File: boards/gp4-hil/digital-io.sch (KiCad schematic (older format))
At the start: 60 parts, among them Q1 SSM6N58NU, Q10 SSM6N58NU, Q2 SSM6N58NU, Q3 SSM6N58NU, Q4 SSM6N58NU, Q5 SSM6N58NU, Q6 SSM6N58NU, Q7 SSM6N58NU, Q8 SSM6N58NU, Q9 SSM6N58NU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

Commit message: Began work on footprint creation for layout.
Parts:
- C57, C58, C59, C60, C61: footprint (none) -> azonenberg_pcb:EIA_0402_CAP_NOSILK
- C62: footprint (none) -> azonenberg_pcb:EIA_0603_CAP_NOSILK
- D1: footprint (none) -> azonenberg_pcb:EIA_0402_LED
- D10, D11, D12, D13, D14, D15, D16, D17, D18, D19, D2, D3, D4, D5, D6, D7, D8, D9: footprint (none) -> azonenberg_pcb:EIA_0603_LED
- Q1, Q10, Q2, Q3, Q4, Q5, Q6, Q7, Q8, Q9: footprint (none) -> azonenberg_pcb:DFN_6_0.65MM_2x2MM_GDS

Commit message: Updated PCB with a lot more component footprints
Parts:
- R81, R82, R83, R84, R85, R86, R87, R88, R89, R90, R91, R92, R93, R94, R95, R96, R97, R98, R99: footprint (none) -> azonenberg_pcb:EIA_0402_RES_NOSILK
- U2: footprint (none) -> azonenberg_pcb:BGA_256_17x17_FULLARRAY_1MM
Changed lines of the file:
@@
 Sheet 7 7
 Title "GreenPak Hardware-In-Loop Test Platform"
-Date "2016-05-19"
+Date "2016-05-20"
 Rev "0.1"
 Comp "Andrew Zonenberg"
@@
 F 0 "U2" H 16350 7350 60  0000 L CNN
 F 1 "XC7A100T-1FTG256C" H 16350 7450 60  0000 L CNN
-F 2 "" H 16350 7550 60  0001 C CNN
+F 2 "azonenberg_pcb:BGA_256_17x17_FULLARRAY_1MM" H 16350 7550 60  0001 C CNN
 F 3 "" H 16350 7550 60  0000 C CNN
 	5    16350 7550
@@
 F 0 "U2" H 19350 7350 60  0000 L CNN
 F 1 "XC7A100T-1FTG256C" H 19350 7450 60  0000 L CNN
-F 2 "" H 19350 7550 60  0001 C CNN
+F 2 "azonenberg_pcb:BGA_256_17x17_FULLARRAY_1MM" H 19350 7550 60  0001 C CNN
 F 3 "" H 19350 7550 60  0000 C CNN
 	6    19350 7550
@@
 F 0 "R81" H 2220 10846 50  0000 L CNN
 F 1 "1K" V 2150 10750 50  0000 L CNN
-F 2 "" V 2080 10800 30  0001 C CNN
+F 2 "azonenberg_pcb:EIA_0402_RES_NOSILK" V 2080 10800 30  0001 C CNN
 F 3 "" H 2150 10800 30  0000 C CNN
 	1    2150 10800
@@
 F 0 "R82" H 6970 9946 50  0000 L CNN
 F 1 "220" V 6900 9850 50  0000 L CNN
-F 2 "" V 6830 9900 30  0001 C CNN
+F 2 "azonenberg_pcb:EIA_0402_RES_NOSILK" V 6830 9900 30  0001 C CNN
 F 3 "" H 6900 9900 30  0000 C CNN
 	1    6900 9900
@@
 F 0 "R84" H 7770 9946 50  0000 L CNN
 F 1 "220" V 7700 9850 50  0000 L CNN
-F 2 "" V 7630 9900 30  0001 C CNN
+F 2 "azonenberg_pcb:EIA_0402_RES_NOSILK" V 7630 9900 30  0001 C CNN
 F 3 "" H 7700 9900 30  0000 C CNN
 	1    7700 9900
@@
 F 0 "R86" H 8570 9946 50  0000 L CNN
 F 1 "220" V 8500 9850 50  0000 L CNN
-F 2 "" V 8430 9900 30  0001 C CNN
+F 2 "azonenberg_pcb:EIA_0402_RES_NOSILK" V 8430 9900 30  0001 C CNN
 F 3 "" H 8500 9900 30  0000 C CNN
 	1    8500 9900
@@
 F 0 "R88" H 9370 9946 50  0000 L CNN
 F 1 "220" V 9300 9850 50  0000 L CNN
-F 2 "" V 9230 9900 30  0001 C CNN
+F 2 "azonenberg_pcb:EIA_0402_RES_NOSILK" V 9230 9900 30  0001 C CNN
 F 3 "" H 9300 9900 30  0000 C CNN
 	1    9300 9900
@@
 F 0 "R90" H 10170 9946 50  0000 L CNN
 F 1 "220" V 10100 9850 50  0000 L CNN
-F 2 "" V 10030 9900 30  0001 C CNN
+F 2 "azonenberg_pcb:EIA_0402_RES_NOSILK" V 10030 9900 30  0001 C CNN
 F 3 "" H 10100 9900 30  0000 C CNN
 	1    10100 9900
@@
 F 0 "R92" H 10970 9946 50  0000 L CNN
 F 1 "220" V 10900 9850 50  0000 L CNN
-F 2 "" V 10830 9900 30  0001 C CNN
+F 2 "azonenberg_pcb:EIA_0402_RES_NOSILK" V 10830 9900 30  0001 C CNN
 F 3 "" H 10900 9900 30  0000 C CNN
 	1    10900 9900
@@
 F 0 "R94" H 11770 9946 50  0000 L CNN
 F 1 "220" V 11700 9850 50  0000 L CNN
-F 2 "" V 11630 9900 30  0001 C CNN
+F 2 "azonenberg_pcb:EIA_0402_RES_NOSILK" V 11630 9900 30  0001 C CNN
 F 3 "" H 11700 9900 30  0000 C CNN
 	1    11700 9900
@@
 F 0 "R96" H 12570 9946 50  0000 L CNN
 F 1 "220" V 12500 9850 50  0000 L CNN
-F 2 "" V 12430 9900 30  0001 C CNN
+F 2 "azonenberg_pcb:EIA_0402_RES_NOSILK" V 12430 9900 30  0001 C CNN
 F 3 "" H 12500 9900 30  0000 C CNN
 	1    12500 9900
@@
 F 0 "R98" H 13370 9946 50  0000 L CNN
 F 1 "220" V 13300 9850 50  0000 L CNN
-F 2 "" V 13230 9900 30  0001 C CNN
+F 2 "azonenberg_pcb:EIA_0402_RES_NOSILK" V 13230 9900 30  0001 C CNN
 F 3 "" H 13300 9900 30  0000 C CNN
 	1    13300 9900
@@
 F 0 "R83" H 6970 11246 50  0000 L CNN
 F 1 "220" V 6900 11150 50  0000 L CNN
-F 2 "" V 6830 11200 30  0001 C CNN
+F 2 "azonenberg_pcb:EIA_0402_RES_NOSILK" V 6830 11200 30  0001 C CNN
 F 3 "" H 6900 11200 30  0000 C CNN
 	1    6900 11200
@@
 F 0 "R85" H 7770 11246 50  0000 L CNN
 F 1 "220" V 7700 11150 50  0000 L CNN
-F 2 "" V 7630 11200 30  0001 C CNN
+F 2 "azonenberg_pcb:EIA_0402_RES_NOSILK" V 7630 11200 30  0001 C CNN
 F 3 "" H 7700 11200 30  0000 C CNN
 	1    7700 11200
@@
 F 0 "R87" H 8570 11246 50  0000 L CNN
 F 1 "220" V 8500 11150 50  0000 L CNN
-F 2 "" V 8430 11200 30  0001 C CNN
+F 2 "azonenberg_pcb:EIA_0402_RES_NOSILK" V 8430 11200 30  0001 C CNN
 F 3 "" H 8500 11200 30  0000 C CNN
 	1    8500 11200
@@
 F 0 "R89" H 9370 11246 50  0000 L CNN
 F 1 "220" V 9300 11150 50  0000 L CNN
-F 2 "" V 9230 11200 30  0001 C CNN
+F 2 "azonenberg_pcb:EIA_0402_RES_NOSILK" V 9230 11200 30  0001 C CNN
 F 3 "" H 9300 11200 30  0000 C CNN
 	1    9300 11200
@@
 F 0 "R91" H 10170 11246 50  0000 L CNN
 F 1 "220" V 10100 11150 50  0000 L CNN
-F 2 "" V 10030 11200 30  0001 C CNN
+F 2 "azonenberg_pcb:EIA_0402_RES_NOSILK" V 10030 11200 30  0001 C CNN
 F 3 "" H 10100 11200 30  0000 C CNN
 	1    10100 11200
@@
 F 0 "R93" H 10970 11246 50  0000 L CNN
 F 1 "220" V 10900 11150 50  0000 L CNN
-F 2 "" V 10830 11200 30  0001 C CNN
+F 2 "azonenberg_pcb:EIA_0402_RES_NOSILK" V 10830 11200 30  0001 C CNN
 F 3 "" H 10900 11200 30  0000 C CNN
 	1    10900 11200
@@
 F 0 "R95" H 11770 11246 50  0000 L CNN
 F 1 "220" V 11700 11150 50  0000 L CNN
-F 2 "" V 11630 11200 30  0001 C CNN
+F 2 "azonenberg_pcb:EIA_0402_RES_NOSILK" V 11630 11200 30  0001 C CNN
 F 3 "" H 11700 11200 30  0000 C CNN
 	1    11700 11200
@@
 F 0 "R97" H 12570 11246 50  0000 L CNN
 F 1 "220" V 12500 11150 50  0000 L CNN
-F 2 "" V 12430 11200 30  0001 C CNN
+F 2 "azonenberg_pcb:EIA_0402_RES_NOSILK" V 12430 11200 30  0001 C CNN
 F 3 "" H 12500 11200 30  0000 C CNN
 	1    12500 11200
@@
 F 0 "R99" H 13370 11246 50  0000 L CNN
 F 1 "220" V 13300 11150 50  0000 L CNN
-F 2 "" V 13230 11200 30  0001 C CNN
+F 2 "azonenberg_pcb:EIA_0402_RES_NOSILK" V 13230 11200 30  0001 C CNN
 F 3 "" H 13300 11200 30  0000 C CNN
 	1    13300 11200

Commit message: More footprint assignments
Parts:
- U15, U16, U17, U18, U19: footprint (none) -> azonenberg_pcb:QFN_14_0.4MM_2x2MM_TI_RUC
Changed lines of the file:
@@
 F 0 "U15" H 1900 1000 60  0000 L CNN
 F 1 "TS3A4751" H 2650 1100 60  0000 C CNN
-F 2 "" H 1900 1050 60  0001 C CNN
+F 2 "azonenberg_pcb:QFN_14_0.4MM_2x2MM_TI_RUC" H 1900 1050 60  0001 C CNN
 F 3 "" H 1900 1050 60  0000 C CNN
 	1    1900 1050
@@
 F 0 "U15" H 1900 1500 60  0000 L CNN
 F 1 "TS3A4751" H 2650 1600 60  0000 C CNN
-F 2 "" H 1900 1550 60  0001 C CNN
+F 2 "azonenberg_pcb:QFN_14_0.4MM_2x2MM_TI_RUC" H 1900 1550 60  0001 C CNN
 F 3 "" H 1900 1550 60  0000 C CNN
 	2    1900 1550
@@
 F 0 "U15" H 1900 2000 60  0000 L CNN
 F 1 "TS3A4751" H 2650 2100 60  0000 C CNN
-F 2 "" H 1900 2050 60  0001 C CNN
+F 2 "azonenberg_pcb:QFN_14_0.4MM_2x2MM_TI_RUC" H 1900 2050 60  0001 C CNN
 F 3 "" H 1900 2050 60  0000 C CNN
 	3    1900 2050
@@
 F 0 "U15" H 1900 2500 60  0000 L CNN
 F 1 "TS3A4751" H 2650 2600 60  0000 C CNN
-F 2 "" H 1900 2550 60  0001 C CNN
+F 2 "azonenberg_pcb:QFN_14_0.4MM_2x2MM_TI_RUC" H 1900 2550 60  0001 C CNN
 F 3 "" H 1900 2550 60  0000 C CNN
 	4    1900 2550
@@
 F 0 "U16" H 1900 3000 60  0000 L CNN
 F 1 "TS3A4751" H 2650 3100 60  0000 C CNN
-F 2 "" H 1900 3050 60  0001 C CNN
+F 2 "azonenberg_pcb:QFN_14_0.4MM_2x2MM_TI_RUC" H 1900 3050 60  0001 C CNN
 F 3 "" H 1900 3050 60  0000 C CNN
 	1    1900 3050
@@
 F 0 "U16" H 1900 3500 60  0000 L CNN
 F 1 "TS3A4751" H 2650 3600 60  0000 C CNN
-F 2 "" H 1900 3550 60  0001 C CNN
+F 2 "azonenberg_pcb:QFN_14_0.4MM_2x2MM_TI_RUC" H 1900 3550 60  0001 C CNN
 F 3 "" H 1900 3550 60  0000 C CNN
 	2    1900 3550
@@
 F 0 "U16" H 1900 4000 60  0000 L CNN
 F 1 "TS3A4751" H 2650 4100 60  0000 C CNN
-F 2 "" H 1900 4050 60  0001 C CNN
+F 2 "azonenberg_pcb:QFN_14_0.4MM_2x2MM_TI_RUC" H 1900 4050 60  0001 C CNN
 F 3 "" H 1900 4050 60  0000 C CNN
 	3    1900 4050
@@
 F 0 "U16" H 1900 4500 60  0000 L CNN
 F 1 "TS3A4751" H 2650 4600 60  0000 C CNN
-F 2 "" H 1900 4550 60  0001 C CNN
+F 2 "azonenberg_pcb:QFN_14_0.4MM_2x2MM_TI_RUC" H 1900 4550 60  0001 C CNN
 F 3 "" H 1900 4550 60  0000 C CNN
 	4    1900 4550
@@
 F 0 "U17" H 1900 5000 60  0000 L CNN
 F 1 "TS3A4751" H 2650 5100 60  0000 C CNN
-F 2 "" H 1900 5050 60  0001 C CNN
+F 2 "azonenberg_pcb:QFN_14_0.4MM_2x2MM_TI_RUC" H 1900 5050 60  0001 C CNN
 F 3 "" H 1900 5050 60  0000 C CNN
 	1    1900 5050
@@
 F 0 "U17" H 1900 5500 60  0000 L CNN
 F 1 "TS3A4751" H 2650 5600 60  0000 C CNN
-F 2 "" H 1900 5550 60  0001 C CNN
+F 2 "azonenberg_pcb:QFN_14_0.4MM_2x2MM_TI_RUC" H 1900 5550 60  0001 C CNN
 F 3 "" H 1900 5550 60  0000 C CNN
 	2    1900 5550
@@
 F 0 "U17" H 1900 6000 60  0000 L CNN
 F 1 "TS3A4751" H 2650 6100 60  0000 C CNN
-F 2 "" H 1900 6050 60  0001 C CNN
+F 2 "azonenberg_pcb:QFN_14_0.4MM_2x2MM_TI_RUC" H 1900 6050 60  0001 C CNN
 F 3 "" H 1900 6050 60  0000 C CNN
 	3    1900 6050
@@
 F 0 "U17" H 1900 6500 60  0000 L CNN
 F 1 "TS3A4751" H 2650 6600 60  0000 C CNN
-F 2 "" H 1900 6550 60  0001 C CNN
+F 2 "azonenberg_pcb:QFN_14_0.4MM_2x2MM_TI_RUC" H 1900 6550 60  0001 C CNN
 F 3 "" H 1900 6550 60  0000 C CNN
 	4    1900 6550
@@
 F 0 "U18" H 1900 7000 60  0000 L CNN
 F 1 "TS3A4751" H 2650 7100 60  0000 C CNN
-F 2 "" H 1900 7050 60  0001 C CNN
+F 2 "azonenberg_pcb:QFN_14_0.4MM_2x2MM_TI_RUC" H 1900 7050 60  0001 C CNN
 F 3 "" H 1900 7050 60  0000 C CNN
 	1    1900 7050
@@
 F 0 "U18" H 1900 7500 60  0000 L CNN
 F 1 "TS3A4751" H 2650 7600 60  0000 C CNN
-F 2 "" H 1900 7550 60  0001 C CNN
+F 2 "azonenberg_pcb:QFN_14_0.4MM_2x2MM_TI_RUC" H 1900 7550 60  0001 C CNN
 F 3 "" H 1900 7550 60  0000 C CNN
 	2    1900 7550
@@
 F 0 "U18" H 1900 8000 60  0000 L CNN
 F 1 "TS3A4751" H 2650 8100 60  0000 C CNN
-F 2 "" H 1900 8050 60  0001 C CNN
+F 2 "azonenberg_pcb:QFN_14_0.4MM_2x2MM_TI_RUC" H 1900 8050 60  0001 C CNN
 F 3 "" H 1900 8050 60  0000 C CNN
 	3    1900 8050
@@
 F 0 "U18" H 1900 8500 60  0000 L CNN
 F 1 "TS3A4751" H 2650 8600 60  0000 C CNN
-F 2 "" H 1900 8550 60  0001 C CNN
+F 2 "azonenberg_pcb:QFN_14_0.4MM_2x2MM_TI_RUC" H 1900 8550 60  0001 C CNN
 F 3 "" H 1900 8550 60  0000 C CNN
 	4    1900 8550
@@
 F 0 "U19" H 1900 9000 60  0000 L CNN
 F 1 "TS3A4751" H 2650 9100 60  0000 C CNN
-F 2 "" H 1900 9050 60  0001 C CNN
+F 2 "azonenberg_pcb:QFN_14_0.4MM_2x2MM_TI_RUC" H 1900 9050 60  0001 C CNN
 F 3 "" H 1900 9050 60  0000 C CNN
 	1    1900 9050
@@
 F 0 "U15" H 7900 1500 60  0000 L CNN
 F 1 "TS3A4751" H 8650 1600 60  0000 C CNN
-F 2 "" H 7900 1550 60  0001 C CNN
+F 2 "azonenberg_pcb:QFN_14_0.4MM_2x2MM_TI_RUC" H 7900 1550 60  0001 C CNN
 F 3 "" H 7900 1550 60  0000 C CNN
 	5    7900 1550
@@
 F 0 "U16" H 7900 2050 60  0000 L CNN
 F 1 "TS3A4751" H 8650 2150 60  0000 C CNN
-F 2 "" H 7900 2100 60  0001 C CNN
+F 2 "azonenberg_pcb:QFN_14_0.4MM_2x2MM_TI_RUC" H 7900 2100 60  0001 C CNN
 F 3 "" H 7900 2100 60  0000 C CNN
 	5    7900 2100
@@
 F 0 "U17" H 7900 2600 60  0000 L CNN
 F 1 "TS3A4751" H 8650 2700 60  0000 C CNN
-F 2 "" H 7900 2650 60  0001 C CNN
+F 2 "azonenberg_pcb:QFN_14_0.4MM_2x2MM_TI_RUC" H 7900 2650 60  0001 C CNN
 F 3 "" H 7900 2650 60  0000 C CNN
 	5    7900 2650
@@
 F 0 "U18" H 7900 3150 60  0000 L CNN
 F 1 "TS3A4751" H 8650 3250 60  0000 C CNN
-F 2 "" H 7900 3200 60  0001 C CNN
+F 2 "azonenberg_pcb:QFN_14_0.4MM_2x2MM_TI_RUC" H 7900 3200 60  0001 C CNN
 F 3 "" H 7900 3200 60  0000 C CNN
 	5    7900 3200
@@
 F 0 "U19" H 7900 3700 60  0000 L CNN
 F 1 "TS3A4751" H 8650 3800 60  0000 C CNN
-F 2 "" H 7900 3750 60  0001 C CNN
+F 2 "azonenberg_pcb:QFN_14_0.4MM_2x2MM_TI_RUC" H 7900 3750 60  0001 C CNN
 F 3 "" H 7900 3750 60  0000 C CNN
 	5    7900 3750

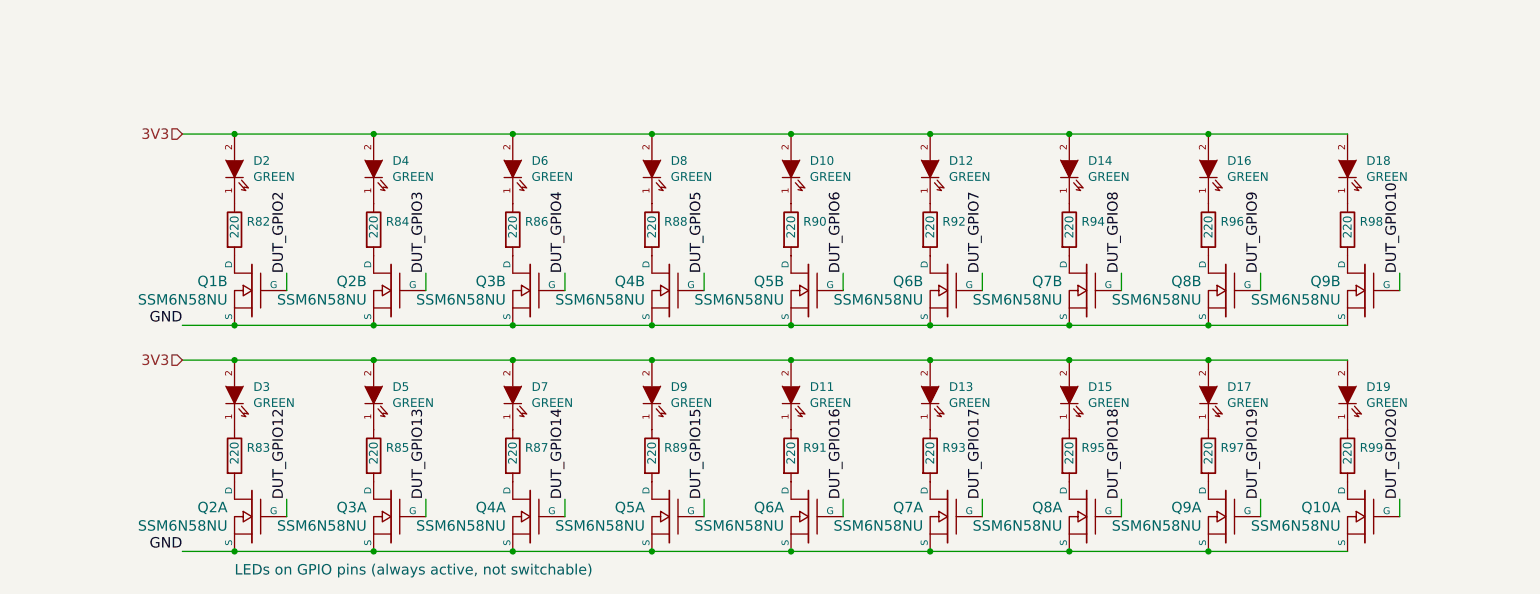
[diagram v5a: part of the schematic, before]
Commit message: Removed redundant LEDs
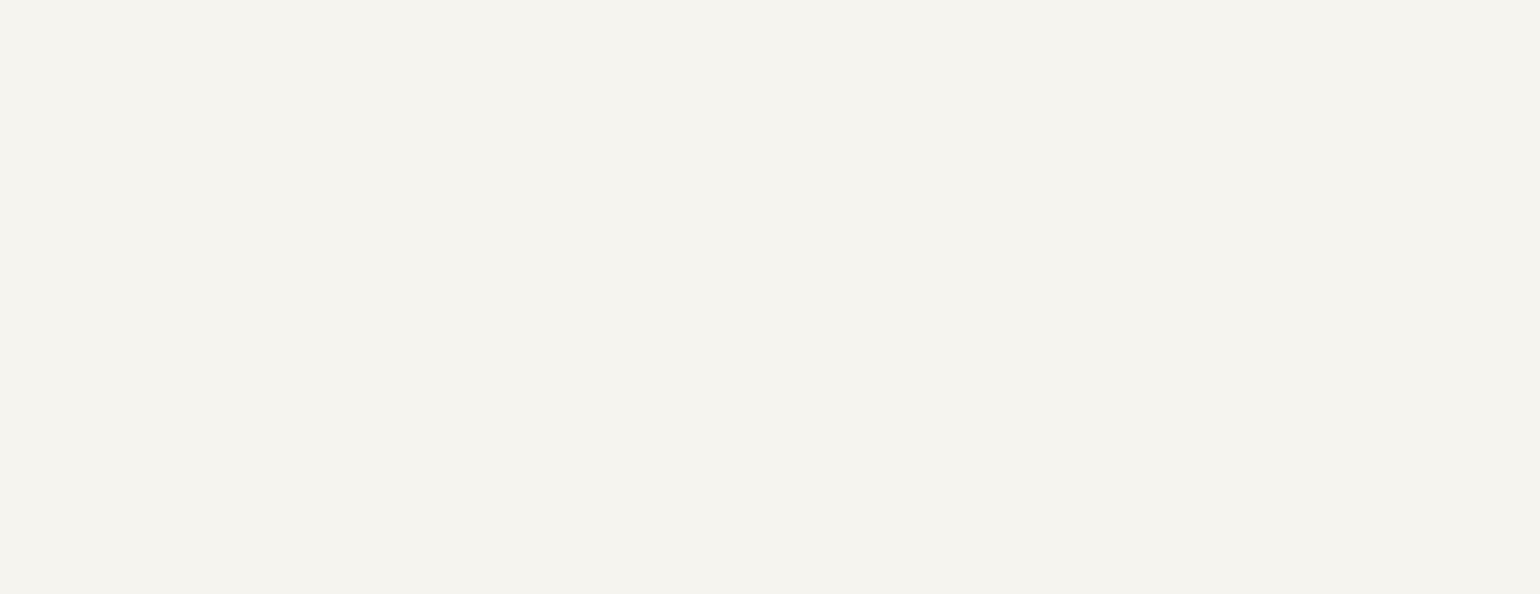
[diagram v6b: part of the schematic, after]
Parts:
- removed D10, D11, D12, D13, D14, D15, D16, D17, D18, D19, D2, D3, D4, D5, D6, D7, D8, D9: GREEN, azonenberg_pcb:EIA_0603_LED, symbol LED
- removed unit 2 of Q1
- removed Q10, Q2, Q3, Q4, Q5, Q6, Q7, Q8, Q9: SSM6N58NU, azonenberg_pcb:DFN_6_0.65MM_2x2MM_GDS, symbol SSM6N58NU_DUAL_NMOS
- removed R82, R83, R84, R85, R86, R87, R88, R89, R90, R91, R92, R93, R94, R95, R96, R97, R98, R99: 220, azonenberg_pcb:EIA_0402_RES_NOSILK, symbol R
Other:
- note removed: "LEDs on GPIO pins (always active, not switchable)"
